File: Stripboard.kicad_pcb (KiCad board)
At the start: 2 copper layers, 25 parts, among them J1 12VAC, J2 EURO POWER HEADER, J3 +12V, J4 0V, J5 -12V, U1 LM7812, U2 LM7912

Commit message: stripbard layout
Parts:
- removed J3: +12V, Connector_PinHeader_2.54mm:PinHeader_1x01_P2.54mm_Vertical
- removed J4: 0V, Connector_PinHeader_2.54mm:PinHeader_1x01_P2.54mm_Vertical
- removed J5: -12V, Connector_PinHeader_2.54mm:PinHeader_1x01_P2.54mm_Vertical
- moved J2 5.08 mm to (147.3, 53.3)
- moved J1 3.81 mm to (45.7, 50.8)
- moved C10 1.27 mm to (121.9, 53.3)
- moved C9 1.27 mm to (121.9, 38.2)
- moved U1 1.27 mm to (113.0, 40.6)
- moved U2 1.27 mm to (113.0, 53.3)
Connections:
- C1 pad 2: /0V -> GNDD
- C10 pad 1: /0V -> GNDD
- C2 pad 1: /0V -> GNDD
- C3 pad 2: /0V -> GNDD
- C4 pad 1: /0V -> GNDD
- C5 pad 2: /0V -> GNDD
- C6 pad 1: /0V -> GNDD
- C7 pad 2: /0V -> GNDD
- C8 pad 1: /0V -> GNDD
- C9 pad 2: /0V -> GNDD
- D5 pad 2: /0V -> GNDD
- D6 pad 1: /0V -> GNDD
- J2 pad 3: /0V -> GNDD
- J2 pad 4: /0V -> GNDD
- J2 pad 5: /0V -> GNDD
- J2 pad 6: /0V -> GNDD
- J2 pad 7: /0V -> GNDD
- J2 pad 8: /0V -> GNDD
- R1 pad 1: /0V -> GNDD
- R2 pad 2: /0V -> GNDD
- U1 pad 2: /0V -> GNDD
- U2 pad 1: /0V -> GNDD
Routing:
- net /0V: track 193.8 -> 0.00 mm, vias 4 -> 0
- net GNDD: track 107.9 -> 298.4 mm, vias 0 -> 8
- net Net-(C10-Pad2): track 80.0 -> 72.4 mm
- net Net-(C9-Pad1): track 65.7 -> 61.8 mm
- net Net-(D1-Pad2): track 17.8 -> 14.0 mm
- net Net-(C2-Pad2): track 67.3 -> 66.0 mm
- net Net-(C1-Pad1): track 67.3 -> 66.0 mm

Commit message: tidy stripboard
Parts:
- moved R1 2.54 mm to (135.9, 50.8)
- moved R2 2.54 mm to (135.9, 38.1)
- moved D5 2.54 mm to (130.8, 38.1)
- moved D6 2.54 mm to (130.8, 50.8)
- moved J2 2.54 mm to (144.8, 53.3)
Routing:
- net Net-(C10-Pad2): track 72.4 -> 63.5 mm
- net GNDD: track 298.4 -> 289.5 mm
- net Net-(C9-Pad1): track 61.8 -> 58.2 mm

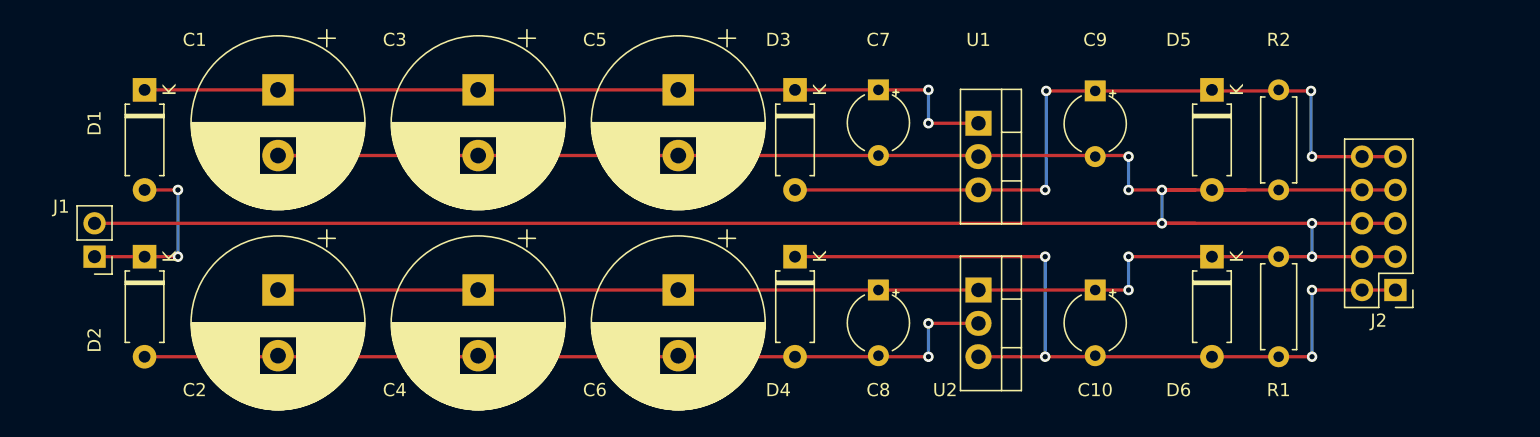
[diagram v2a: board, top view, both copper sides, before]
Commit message: flip sides
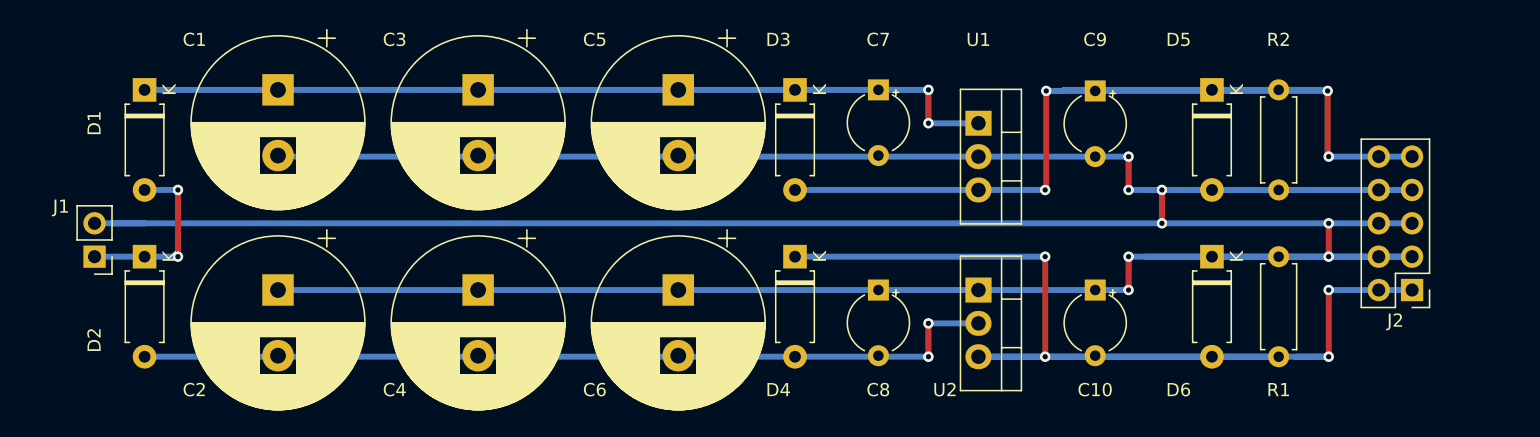
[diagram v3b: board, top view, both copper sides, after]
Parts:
- moved J2 1.27 mm to (146.1, 53.3)
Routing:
- net GNDD: track 289.5 -> 326.4 mm
- net Net-(C10-Pad2): track 63.5 -> 90.2 mm
- net Net-(C9-Pad1): track 58.2 -> 81.0 mm
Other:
- net class Default: trace_width 0.25 -> 0.45
- rule trace_min: 0.2 -> 0.45
